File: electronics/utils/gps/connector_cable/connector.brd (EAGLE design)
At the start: 17.4 x 22.9 mm, 2 parts, among them X1 87758-2016

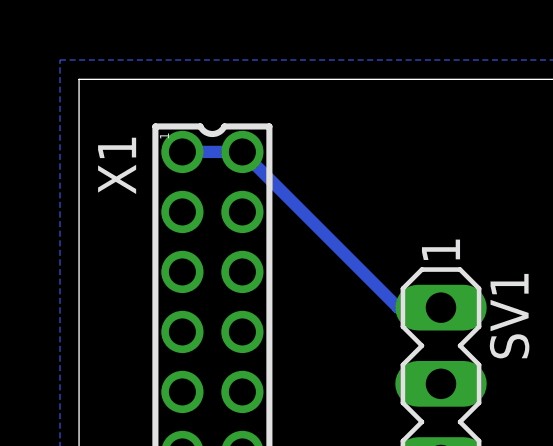
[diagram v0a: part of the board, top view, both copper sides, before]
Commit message: adicionado nota do numero 1 na placa para facilitar montagem
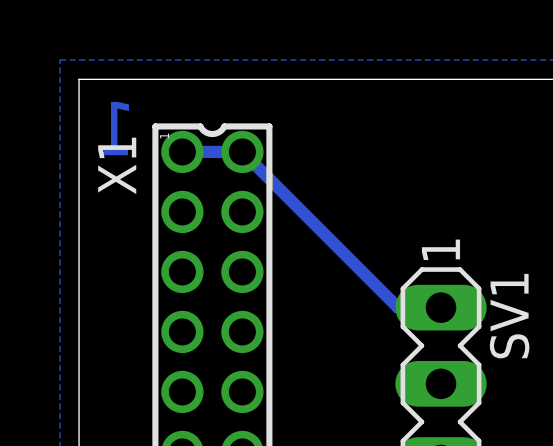
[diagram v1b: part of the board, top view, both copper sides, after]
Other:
- board text added: "1"
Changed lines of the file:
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@@
 <wire x1="19.355" y1="22.85" x2="1.905" y2="22.85" width="0" layer="20"/>
 <wire x1="1.905" y1="22.85" x2="1.905" y2="0" width="0" layer="20"/>
+<text x="3.81" y="20.32" size="1.778" layer="16" rot="MR0">1</text>
 </plain>
 <attributes>
@@
 <wire x1="5.35" y1="8.43" x2="5.255" y2="8.43" width="0.4064" layer="16"/>
 <wire x1="5.255" y1="8.43" x2="4.445" y2="7.62" width="0.4064" layer="16"/>
-<wire x1="4.445" y1="7.62" x2="7.35" y2="6.43" width="0" layer="19" extent="1-16"/>
 </signal>
 <signal name="TX">

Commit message: atualizando computador
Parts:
- moved X1 1.80 mm to (7.62, 10.2)
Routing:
- net TX: track 32.4 -> 41.1 mm
- net VCC: track 10.8 -> 8.97 mm
- net RX: track 7.78 -> 5.99 mm
- net GND: track 1.24 -> 0.00 mm
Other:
- board size 17.4 x 22.9 mm -> 19.4 x 26 mm
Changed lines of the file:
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@@
 <board>
 <plain>
-<wire x1="1.905" y1="0" x2="19.355" y2="0" width="0" layer="20"/>
-<wire x1="19.355" y1="0" x2="19.355" y2="22.85" width="0" layer="20"/>
-<wire x1="19.355" y1="22.85" x2="1.905" y2="22.85" width="0" layer="20"/>
-<wire x1="1.905" y1="22.85" x2="1.905" y2="0" width="0" layer="20"/>
-<text x="3.81" y="20.32" size="1.778" layer="16" rot="MR0">1</text>
+<wire x1="1.27" y1="-1.905" x2="20.625" y2="-1.905" width="0" layer="20"/>
+<wire x1="20.625" y1="-1.905" x2="20.625" y2="24.12" width="0" layer="20"/>
+<wire x1="20.625" y1="24.12" x2="1.27" y2="24.12" width="0" layer="20"/>
+<wire x1="1.27" y1="24.12" x2="1.27" y2="-1.905" width="0" layer="20"/>
+<text x="2.54" y="22.225" size="1.778" layer="16" rot="MR0">1</text>
 </plain>
 <attributes>
@@
 <pass name="Default">
 <param name="RoutingGrid" value="50mil"/>
-<param name="tpViaShape" value="round"/>
+<param name="tpViaShape" value="octagon"/>
 <param name="PrefDir.1" value="|"/>
 <param name="PrefDir.2" value="0"/>
@@
 </autorouter>
 <elements>
-<element name="X1" library="con-molex" package="87758-2016" value="87758-2016" x="6.35" y="11.43" rot="R270">
-<attribute name="OC_NEWARK" value="25M5677" x="1.27" y="-11.43" size="1.778" layer="27" rot="R270" display="off"/>
-<attribute name="MPN" value="87758-2016" x="1.27" y="-11.43" size="1.778" layer="27" rot="R270" display="off"/>
-<attribute name="MF" value="" x="1.27" y="-11.43" size="1.778" layer="27" rot="R270" display="off"/>
-<attribute name="OC_FARNELL" value="7472374" x="1.27" y="-11.43" size="1.778" layer="27" rot="R270" display="off"/>
+<element name="X1" library="con-molex" package="87758-2016" value="87758-2016" x="7.62" y="10.16" rot="R270">
+<attribute name="OC_NEWARK" value="25M5677" x="2.54" y="-12.7" size="1.778" layer="27" rot="R270" display="off"/>
+<attribute name="MPN" value="87758-2016" x="2.54" y="-12.7" size="1.778" layer="27" rot="R270" display="off"/>
+<attribute name="MF" value="" x="2.54" y="-12.7" size="1.778" layer="27" rot="R270" display="off"/>
+<attribute name="OC_FARNELL" value="7472374" x="2.54" y="-12.7" size="1.778" layer="27" rot="R270" display="off"/>
 </element>
 <element name="SV1" library="con-lstb" package="MA04-1" value="" x="13.97" y="11.43" rot="R270">
@@
 <contactref element="SV1" pad="1"/>
 <wire x1="13.97" y1="15.24" x2="12.54" y2="15.24" width="0.4064" layer="16"/>
-<wire x1="12.54" y1="15.24" x2="7.35" y2="20.43" width="0.4064" layer="16"/>
-<wire x1="7.35" y1="20.43" x2="5.35" y2="20.43" width="0.4064" layer="16"/>
+<wire x1="12.54" y1="15.24" x2="8.62" y2="19.16" width="0.8001" layer="16"/>
+<wire x1="8.62" y1="19.16" x2="6.62" y2="19.16" width="0.8001" layer="16"/>
 </signal>
 <signal name="GND">
@@
 <contactref element="X1" pad="18"/>
 <contactref element="SV1" pad="2"/>
-<polygon width="0.4064" layer="16">
-<vertex x="1.27" y="-0.635"/>
+<polygon width="0.4064" layer="16" isolate="0.4064">
+<vertex x="1.27" y="-1.27"/>
 <vertex x="1.27" y="23.495"/>
 <vertex x="20.32" y="23.495"/>
-<vertex x="20.32" y="-0.635"/>
+<vertex x="20.32" y="-1.27"/>
 </polygon>
-<wire x1="5.35" y1="8.43" x2="5.255" y2="8.43" width="0.4064" layer="16"/>
-<wire x1="5.255" y1="8.43" x2="4.445" y2="7.62" width="0.4064" layer="16"/>
+<wire x1="6.62" y1="7.16" x2="8.62" y2="11.16" width="0" layer="19" extent="1-1"/>
 </signal>
 <signal name="TX">
 <contactref element="X1" pad="11"/>
 <contactref element="SV1" pad="3"/>
-<wire x1="13.97" y1="10.16" x2="15.875" y2="10.16" width="0.4064" layer="16"/>
-<wire x1="15.875" y1="10.16" x2="16.51" y2="9.525" width="0.4064" layer="16"/>
-<wire x1="16.51" y1="9.525" x2="16.51" y2="5.08" width="0.4064" layer="16"/>
-<wire x1="16.51" y1="5.08" x2="12.065" y2="0.635" width="0.4064" layer="16"/>
-<wire x1="12.065" y1="0.635" x2="4.445" y2="0.635" width="0.4064" layer="16"/>
-<wire x1="4.445" y1="0.635" x2="3.175" y2="1.905" width="0.4064" layer="16"/>
-<wire x1="3.175" y1="1.905" x2="3.175" y2="8.255" width="0.4064" layer="16"/>
-<wire x1="3.175" y1="8.255" x2="5.35" y2="10.43" width="0.4064" layer="16"/>
+<wire x1="13.97" y1="10.16" x2="15.24" y2="10.16" width="0.4064" layer="16"/>
+<wire x1="15.24" y1="10.16" x2="17.78" y2="12.7" width="0.8001" layer="16"/>
+<wire x1="17.78" y1="12.7" x2="17.78" y2="20.32" width="0.8001" layer="16"/>
+<wire x1="17.78" y1="20.32" x2="16.51" y2="21.59" width="0.8001" layer="16"/>
+<wire x1="16.51" y1="21.59" x2="5.08" y2="21.59" width="0.8001" layer="16"/>
+<wire x1="5.08" y1="21.59" x2="3.81" y2="20.32" width="0.8001" layer="16"/>
+<wire x1="3.81" y1="20.32" x2="3.81" y2="10.16" width="0.8001" layer="16"/>
+<wire x1="3.81" y1="10.16" x2="5.08" y2="8.89" width="0.8001" layer="16"/>
+<wire x1="5.08" y1="8.89" x2="6.35" y2="8.89" width="0.8001" layer="16"/>
+<wire x1="6.35" y1="8.89" x2="6.62" y2="9.16" width="0.4064" layer="16"/>
 </signal>
 <signal name="RX">
 <contactref element="X1" pad="12"/>
 <contactref element="SV1" pad="4"/>
-<wire x1="13.97" y1="7.62" x2="10.16" y2="7.62" width="0.4064" layer="16"/>
-<wire x1="10.16" y1="7.62" x2="7.35" y2="10.43" width="0.4064" layer="16"/>
+<wire x1="13.97" y1="7.62" x2="10.16" y2="7.62" width="0.8001" layer="16"/>
+<wire x1="10.16" y1="7.62" x2="8.62" y2="9.16" width="0.8001" layer="16"/>
 </signal>
 </signals>
